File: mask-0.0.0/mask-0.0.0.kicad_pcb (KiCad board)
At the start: 2 copper layers, 165 x 113 mm, 108 parts, among them J1 Conn_02x05_Counter_Clockwise, J2 Conn_ARM_JTAG_SWD_10, J3 USB_C_Receptacle_USB2.0, J4 USB_C_Receptacle_USB2.0, Q1 IRLML2502, SW1 SW_Push, SW10 SW_Push, SW11 SW_Push, SW12 SW_Push, SW13 SW_Push, SW13_1 SW_Push, SW14 SW_Push, SW15 SW_Push, SW16 SW_Push, SW17 SW_Push, SW18 SW_Push, SW19 SW_Push, SW2 SW_Push, SW20 SW_Push, SW20_1 SW_Push, SW21 SW_Push, SW22 SW_Push, SW23 SW_Push, SW24 SW_Push, SW25 SW_Push, SW26 SW_Push, SW27 SW_Push, SW27_1 SW_Push, SW28 SW_Push, SW29 SW_Push, SW3 SW_Push, SW30 SW_Push, SW31 SW_Push, SW32 SW_Push, SW33 SW_Push, SW34 SW_Push, SW35 SW_Push, SW36 SW_Push, SW37 SW_Push, SW4 SW_Push, SW5 SW_Push, SW6 SW_Push, SW7 SW_Push, SW8 SW_Push, SW9 SW_Push, U1 NORA-B10x, U2 MCP1703A-3302_SOT23

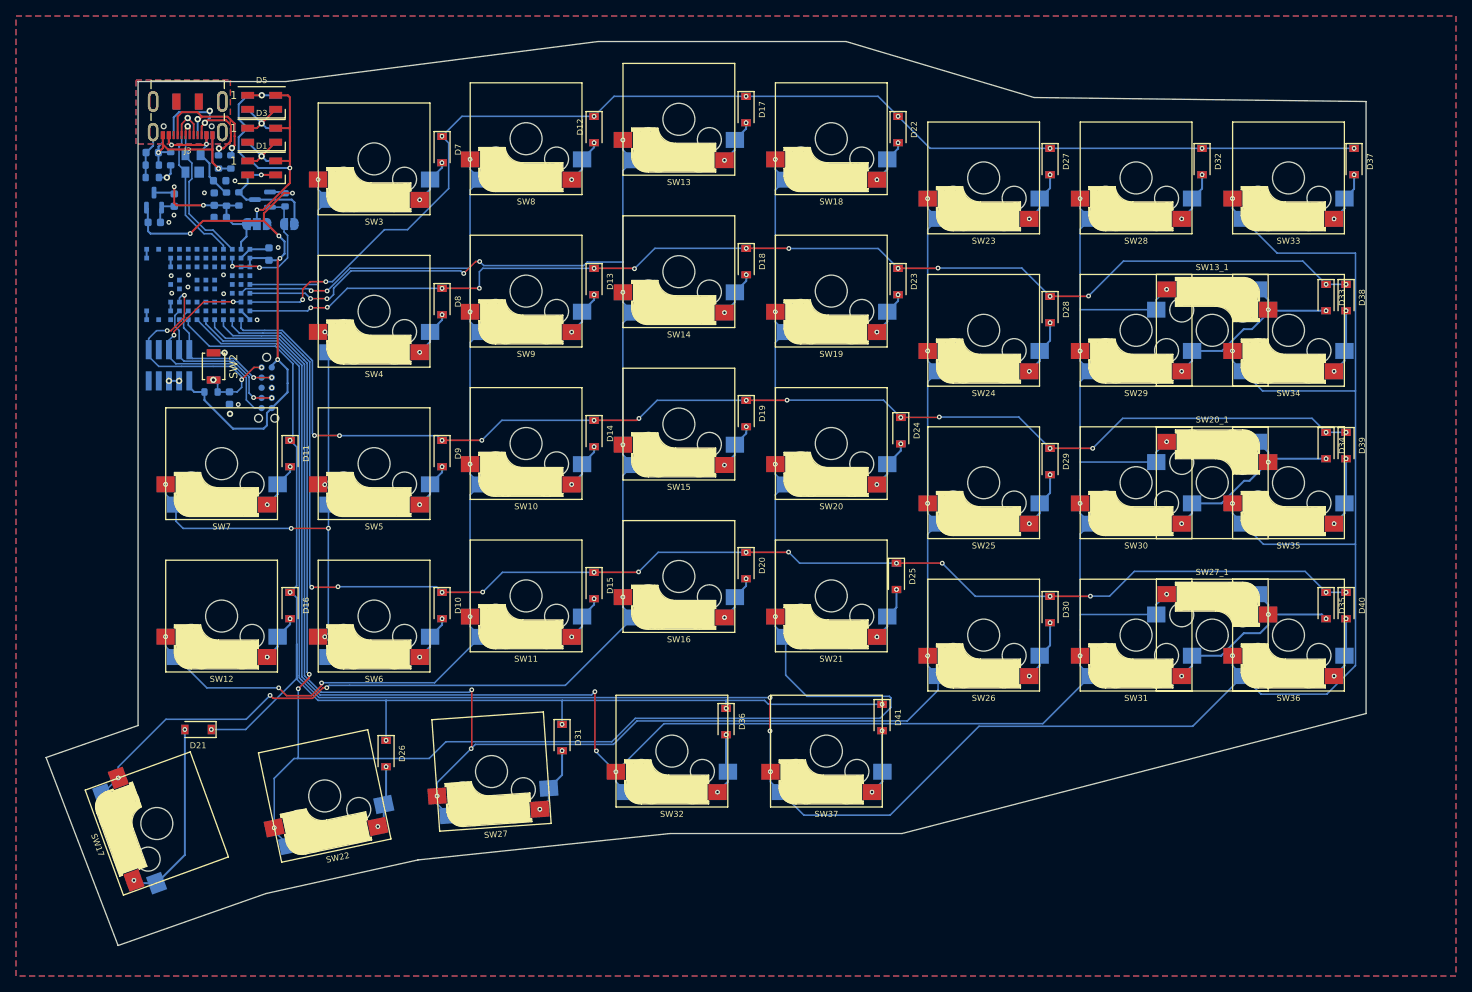
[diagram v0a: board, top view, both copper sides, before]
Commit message: mask-0.0.0: optimize routing, via stitching
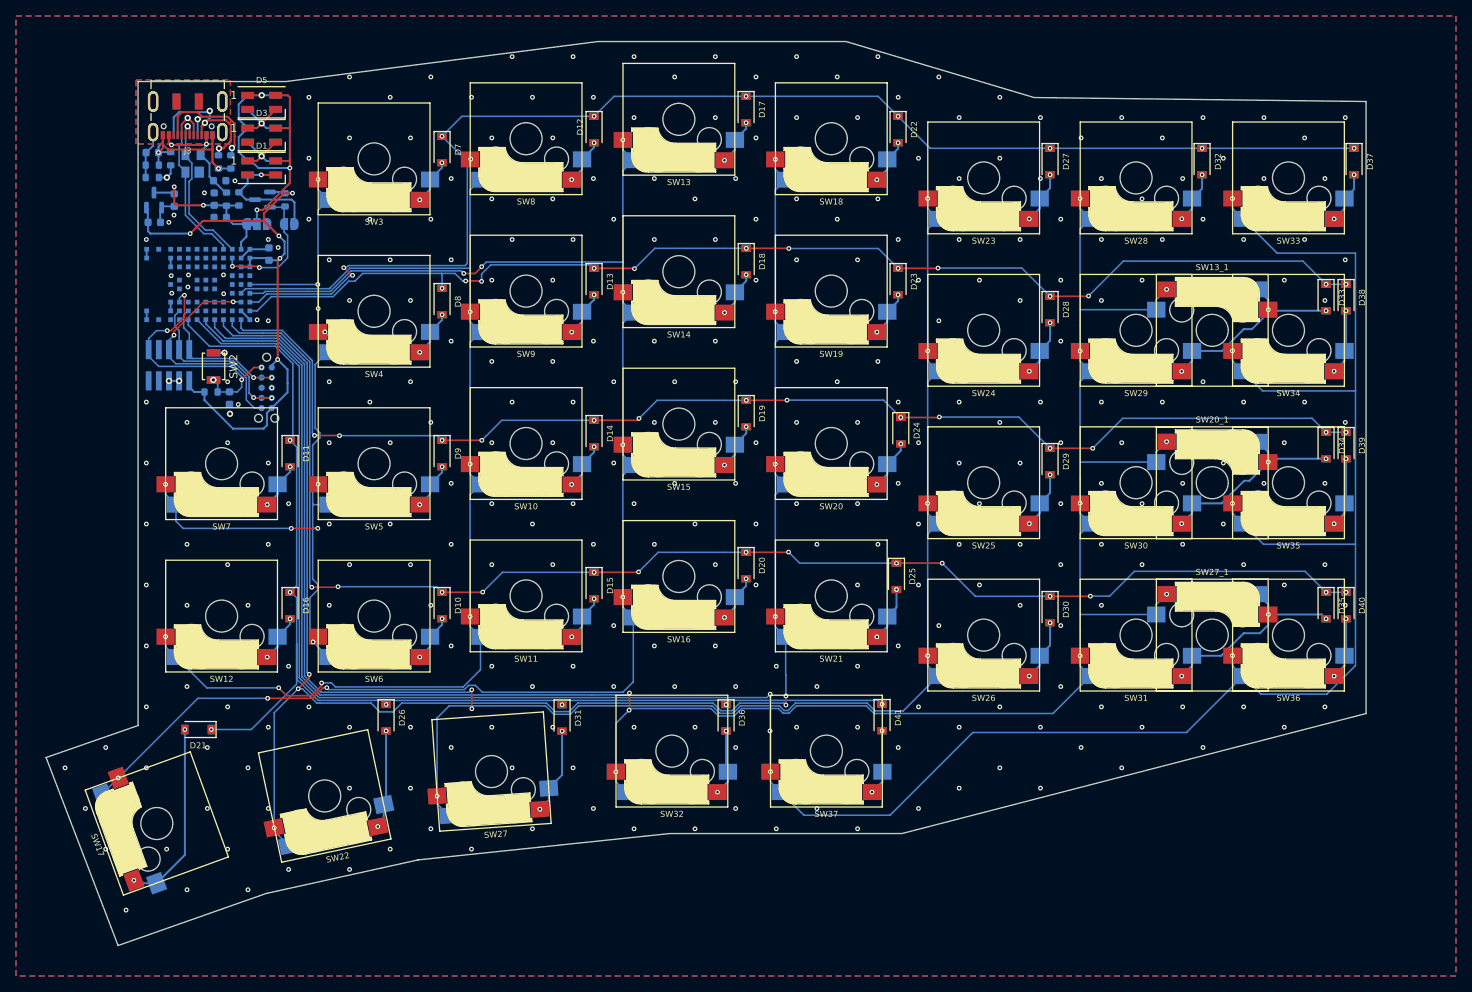
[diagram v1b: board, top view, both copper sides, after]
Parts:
- moved D26 4.48 mm to (71.5, 142.0)
- moved D31 2.45 mm to (93.5, 142.1)
- moved D36 0.46 mm to (114.0, 142.0)
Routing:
- net COL3: track 237.0 -> 212.5 mm, vias 7 -> 9
- net ROW0: track 157.1 -> 167.3 mm
- net ROW4: track 157.8 -> 149.5 mm
- net Net-(D26-Pad2): track 7.90 -> 12.4 mm
- net COL0: track 95.2 -> 99.5 mm, vias 7 -> 9
- net COL2: track 190.1 -> 193.2 mm, vias 11 -> 9
- net COL1: track 140.2 -> 142.7 mm, vias 9 -> 7
- net Net-(D31-Pad2): track 8.47 -> 10.9 mm
- net ROW1: track 147.0 -> 149.4 mm, vias 14 -> 13
- net COL4: track 219.7 -> 221.9 mm
- net COL5: track 271.1 -> 272.0 mm
- net COL6: track 319.0 -> 319.6 mm
- net GND: vias 19 -> 324

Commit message: mask-0.0.0: add text to copper, change fill-zone parameter
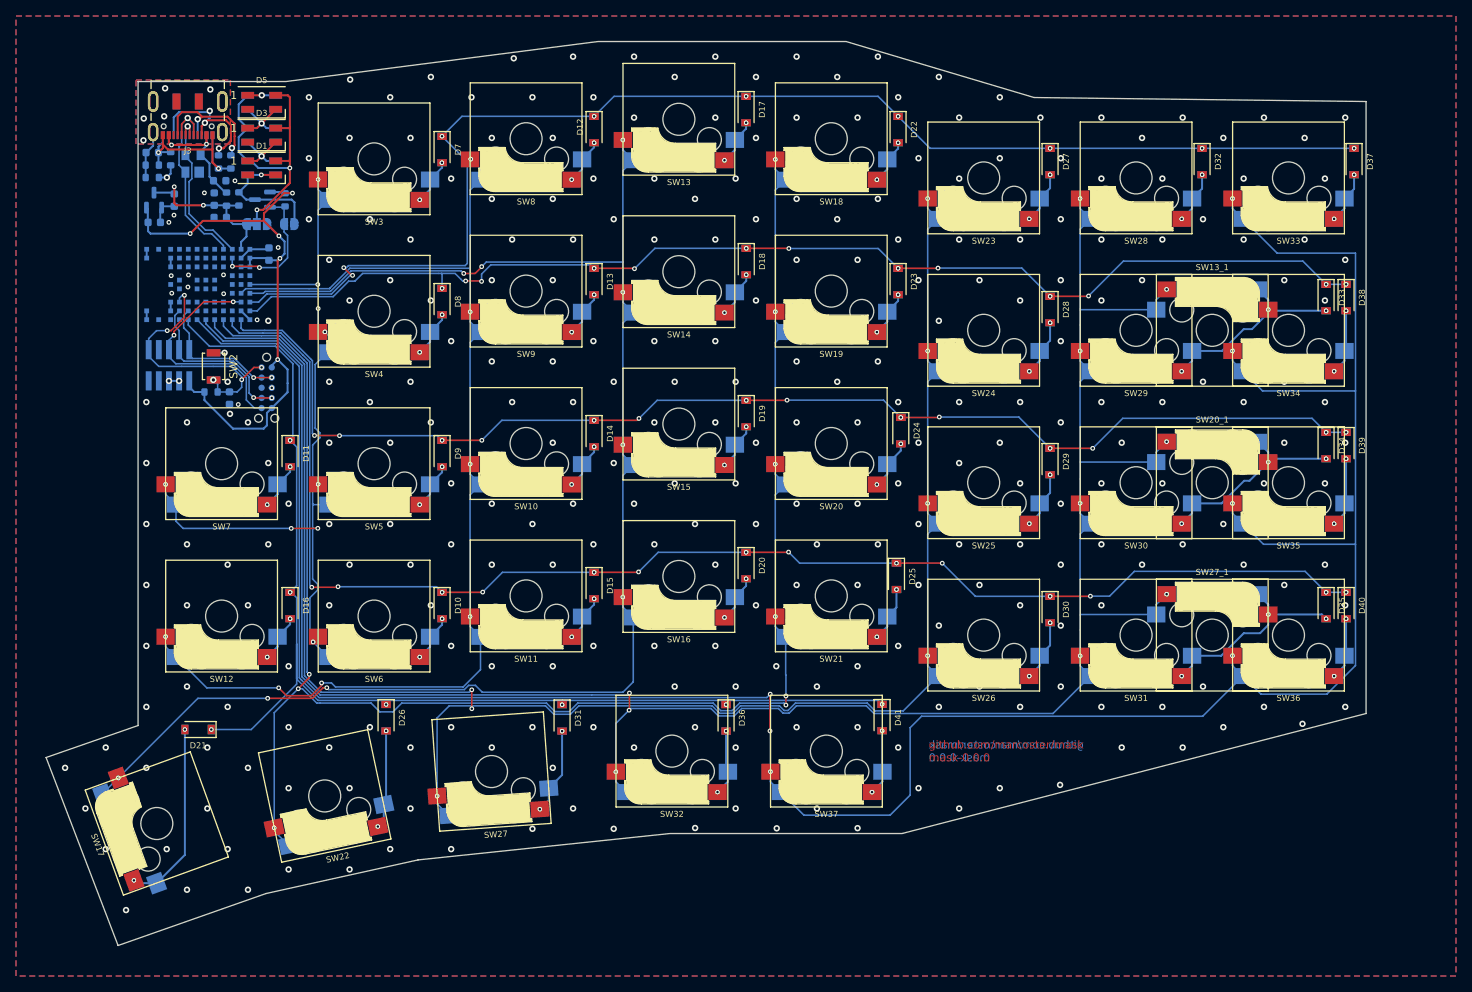
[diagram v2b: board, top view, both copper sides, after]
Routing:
- net COL6: track 319.6 -> 324.6 mm
- net GND: vias 324 -> 308
- net /Usb/USB_SHIELD: vias 0 -> 5
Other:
- board text added: "github.com/marcoster/mask mask-0.0.0"
